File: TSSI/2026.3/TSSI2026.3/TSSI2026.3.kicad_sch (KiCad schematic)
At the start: 31 parts, among them J1 T2M-105-01-X-D-TH-DS, J2 Conn_01x02, Q1 IRLZ34N, T555 Test555, U1 LM555xN, U2 IRLZ34N, U3 IRLZ34N, U4 4001, U5 4069

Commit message: Change TSSI2026.3
Deleted the whole schematic ong
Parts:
- removed DEBUG1: BMS, LED_THT:LED_D4.0mm, symbol Device:LED
- removed DEBUG2: IMD, LED_THT:LED_D4.0mm, symbol Device:LED
- removed IMD1: TestIMD, Connector_PinHeader_1.00mm:PinHeader_1x01_P1.00mm_Vertical, symbol Connector:Conn_01x01_Pin
- removed J1: T2M-105-01-X-D-TH-DS, T2M-105-01-X-D-TH-DS:SAMTEC_T2M-105-01-X-D-TH-DS, symbol T2M-105-01-X-D-TH-DS:T2M-105-01-X-D-TH-DS
- removed R3: 50, Resistor_SMD:R_0805_2012Metric, symbol Device:R_US
- removed R9: 20k, Resistor_SMD:R_0805_2012Metric, symbol Device:R_US
- removed U2: IRLZ34N, Anteater-Electric-Racing electrical-pcbs main TSSI-2026.2_KiCad_Parts_IRLZ34N:TO-220_2_, symbol IRLZ34N:IRLZ34N
- removed U4: 4001, Package_SO:SOIC-14_3.9x8.7mm_P1.27mm, symbol 4xxx:4001
- removed U5: 4069, Package_SO:SOIC-14_3.9x8.7mm_P1.27mm, symbol 4xxx:4069
- added D1: DEBUGLatch, LED_THT:LED_D4.0mm, symbol Device:LED
- added J1: Conn_02x02, Connector_Molex:Molex_Mini-Fit_Jr_5566-04A2_2x02_P4.20mm_Vertical, symbol Connector_Generic:Conn_02x02_Counter_Clockwise
- added Q2, Q3: IRLZ34N, Anteater-Electric-Racing electrical-pcbs main TSSI-2026.2_KiCad_Parts_IRLZ34N:TO-220_2_, symbol IRLZ34N:IRLZ34N
- R1: value 22k -> 10k
- R2: value 20k -> 22k
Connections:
- net GLV: now also R1.1, J1.1 (Pin_1); no longer R1.2
- net GND: now also D1.1 (K), J1.2 (Pin_2), Q2.OUT, Q3.OUT
- net at Q1.IN: now also R1.2, Q2.IN, Q3.GND
- net at R5.2, U1.4 (R): now also Q2.GND
- net Latch_12V_Safe: now reaches R2.1
- net Latch_12V_Safe: now also BMS1.1 (Pin_1), J1.3 (Pin_3), Q3.IN
- removed net BMS_FAULT: BMS1.1 (Pin_1), R1.1
- net IMD_FAULT: no longer names the net of R2.2
- net IMD_FAULT: now also D1.2 (A)
- no-connect marks 7 -> 1
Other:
- moved on the sheet: BMS1, C1, C2, C3, GLV1, GND1, H1, H2, H3, H4, J2, Q1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

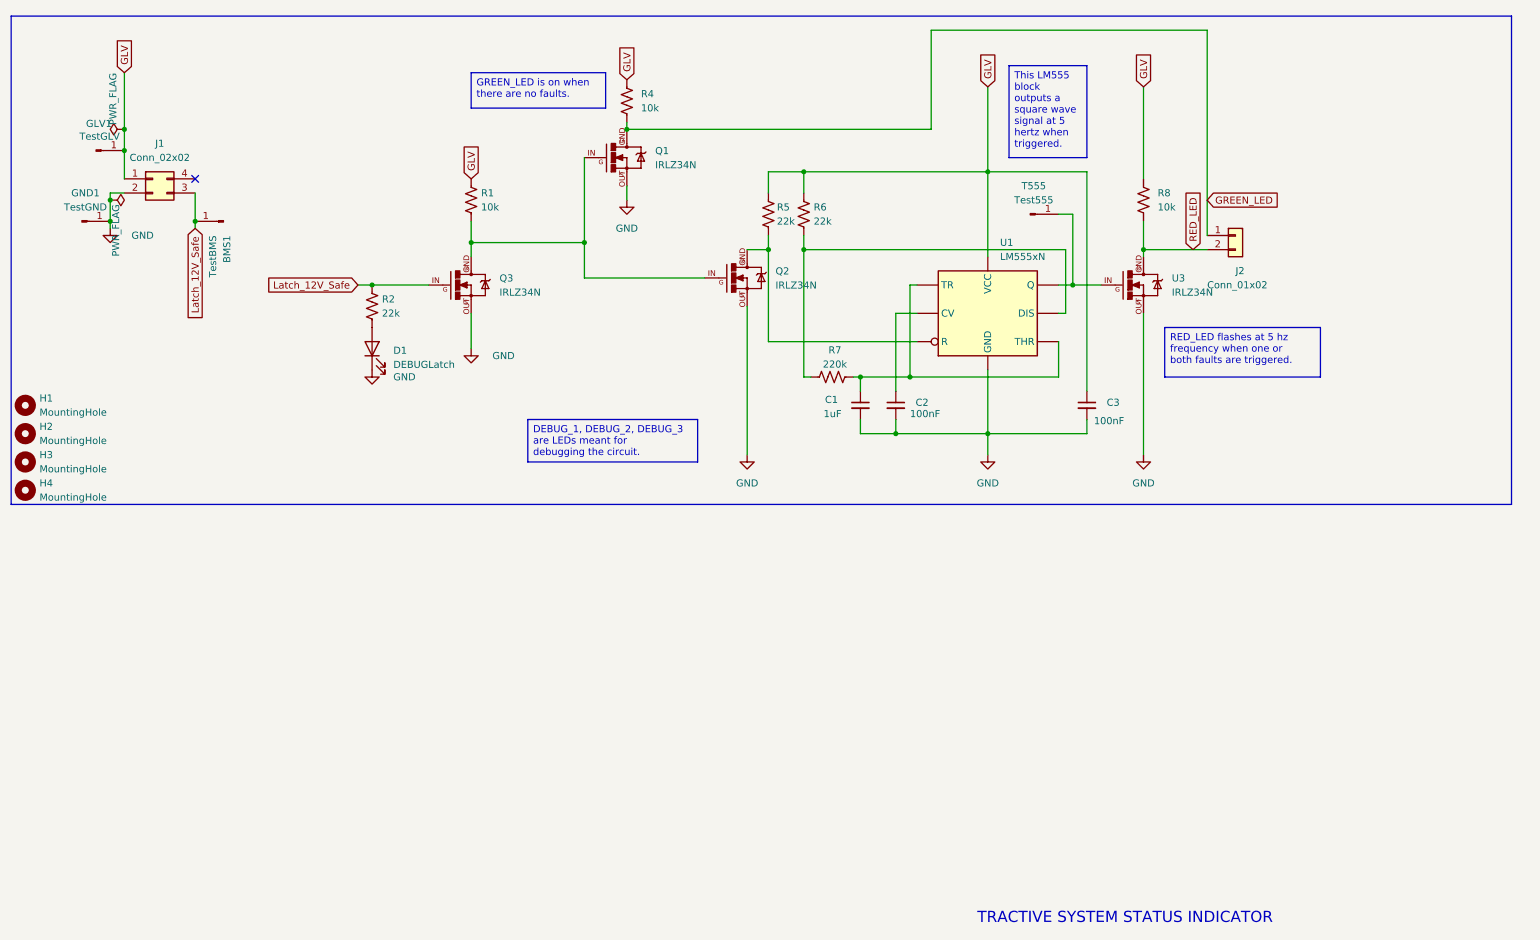
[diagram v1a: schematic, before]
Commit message: Redesign TSSI
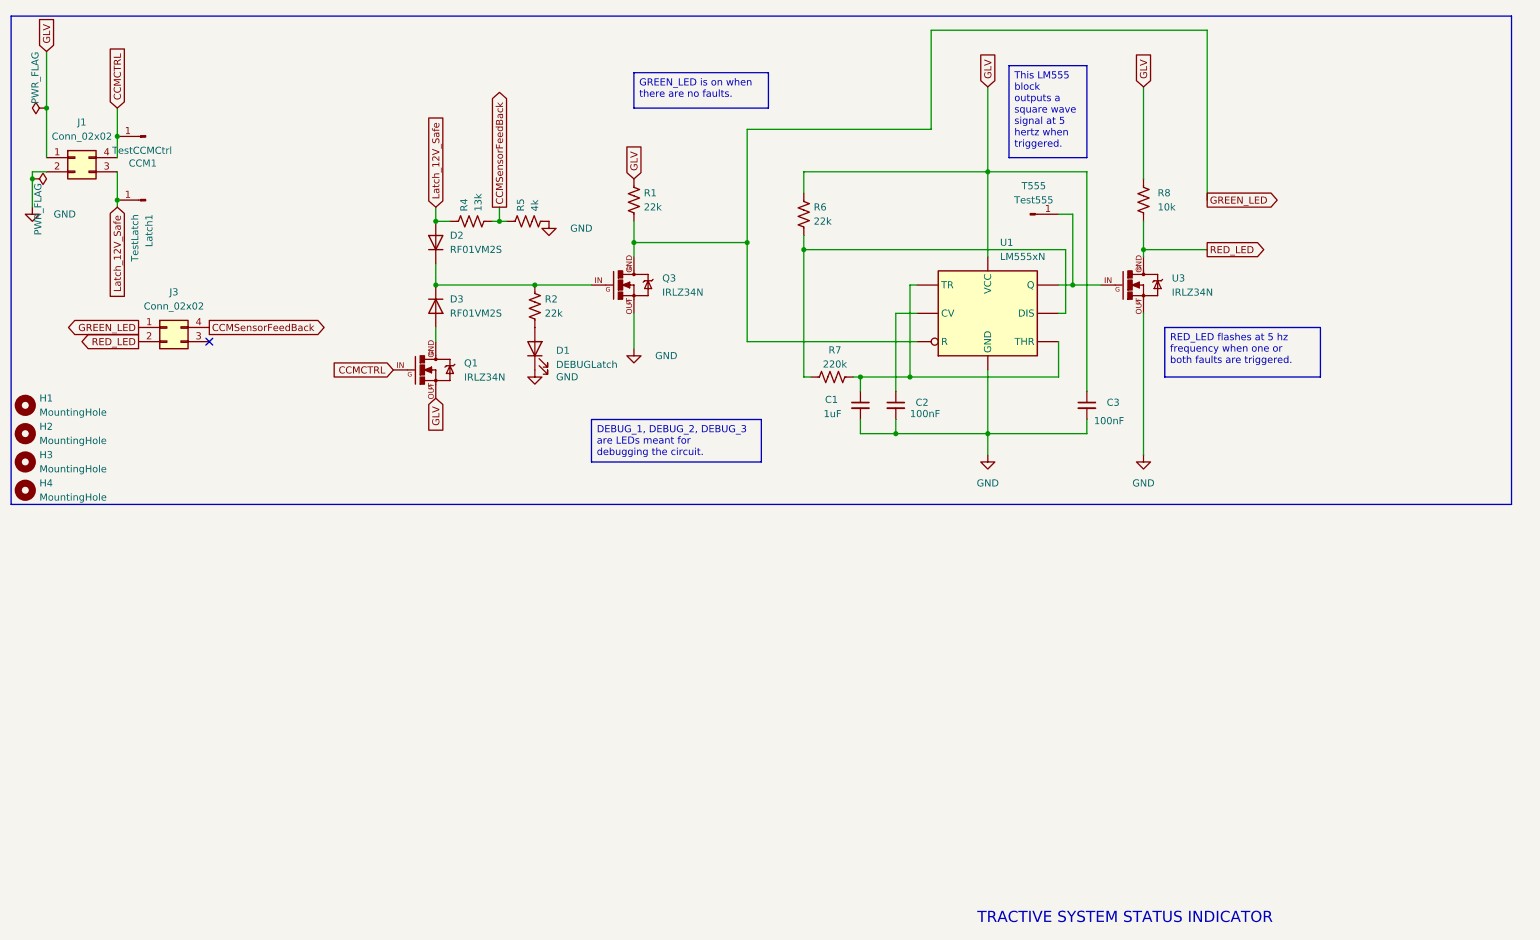
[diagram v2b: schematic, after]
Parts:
- removed GLV1: TestGLV, Connector_PinHeader_1.00mm:PinHeader_1x01_P1.00mm_Vertical, symbol Connector:Conn_01x01_Pin
- removed GND1: TestGND, Connector_PinHeader_1.00mm:PinHeader_1x01_P1.00mm_Vertical, symbol Connector:Conn_01x01_Pin
- removed J2: Conn_01x02, Connector_Molex:Molex_Mini-Fit_Jr_5566-02A_2x01_P4.20mm_Vertical, symbol Connector_Generic:Conn_01x02
- removed Q2: IRLZ34N, Anteater-Electric-Racing electrical-pcbs main TSSI-2026.2_KiCad_Parts_IRLZ34N:TO-220_2_, symbol IRLZ34N:IRLZ34N
- added CCM1: TestCCMCtrl, Connector_PinHeader_1.00mm:PinHeader_1x01_P1.00mm_Vertical, symbol Connector:Conn_01x01_Pin
- added D2, D3: RF01VM2S, Diode_SMD:D_0805_2012Metric, symbol Diode:RF01VM2S
- added J3: Conn_02x02, Connector_Molex:Molex_Mini-Fit_Jr_5566-04A2_2x02_P4.20mm_Vertical, symbol Connector_Generic:Conn_02x02_Counter_Clockwise
- Latch1: renamed from BMS1; value TestBMS -> TestLatch
- R1: value 10k -> 22k
- R4: value 10k -> 13k
- R5: value 22k -> 4k
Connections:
- net GLV: now also Q1.OUT; no longer R4.1, R5.1
- net GND: now also R5.2; no longer Q1.OUT
- net GREEN_LED: now also Q3.GND, R1.2, U1.4 (R), J3.1 (Pin_1); no longer Q1.GND, R4.2
- net Latch_12V_Safe: now also R4.1, D2.2 (A); no longer Q3.IN, R2.1
- net RED_LED: now also J3.2 (Pin_2)
- net CCMCTRL: now reaches J1.4 (Pin_4)
- net CCMCTRL: now also Q1.IN, CCM1.1 (Pin_1)
- new net: D3.2 (A), Q1.GND
- new net: D2.1 (K), D3.1 (K), Q3.IN, R2.1
- new net CCMSensorFeedBack: J3.4 (Pin_4), R4.2, R5.1
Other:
- moved on the sheet: D1, J1, Latch1, Q3, R1, R2

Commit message: Swapped NMOS at bottom
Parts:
- Q1, Q3, U3: footprint Anteater-Electric-Racing electrical-pcbs main TSSI-2026.2_KiCad_Parts_IRLZ34N:TO-220_2_ -> IRLZ34N:TO-220_2_
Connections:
- net GLV: now also Q1.GND; no longer Q1.OUT
- net at D3.2 (A): now also Q1.OUT; no longer Q1.GND
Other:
- moved on the sheet: D2, D3, Q1
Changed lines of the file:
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@@
 	)
 	(junction
-		(at 90.17 62.23)
+		(at 82.55 62.23)
 		(diameter 0)
 		(color 0 0 0 0)
@@
 	)
 	(junction
-		(at 90.17 50.8)
+		(at 82.55 50.8)
 		(diameter 0)
 		(color 0 0 0 0)
@@
 	(wire
 		(pts
-			(xy 90.17 48.26) (xy 90.17 50.8)
+			(xy 82.55 48.26) (xy 82.55 50.8)
 		)
 		(stroke
@@
 	(wire
 		(pts
-			(xy 90.17 69.85) (xy 90.17 72.39)
+			(xy 82.55 69.85) (xy 82.55 72.39)
 		)
 		(stroke
@@
 	(wire
 		(pts
-			(xy 90.17 62.23) (xy 107.95 62.23)
+			(xy 82.55 62.23) (xy 107.95 62.23)
 		)
 		(stroke
@@
 	(wire
 		(pts
-			(xy 90.17 50.8) (xy 92.71 50.8)
+			(xy 82.55 50.8) (xy 92.71 50.8)
 		)
 		(stroke
@@
 	(wire
 		(pts
-			(xy 90.17 58.42) (xy 90.17 62.23)
+			(xy 82.55 58.42) (xy 82.55 62.23)
 		)
 		(stroke
@@
 	(global_label "CCMCTRL"
 		(shape input)
-		(at 82.55 77.47 180)
+		(at 90.17 77.47 0)
 		(fields_autoplaced yes)
 		(effects
@@
 				(size 1.27 1.27)
 			)
-			(justify right)
+			(justify left)
 		)
 		(property "Intersheetrefs" "${INTERSHEET_REFS}"
-			(at 71.0377 77.47 0)
-			(effects
-				(font
-					(size 1.27 1.27)
-				)
-				(justify right)
+			(at 101.6823 77.47 0)
+			(effects
+				(font
+					(size 1.27 1.27)
+				)
+				(justify left)
 				(hide yes)
 			)
@@
 	(global_label "Latch_12V_Safe"
 		(shape input)
-		(at 90.17 48.26 90)
+		(at 82.55 48.26 90)
 		(fields_autoplaced yes)
 		(effects
@@
 		)
 		(property "Intersheetrefs" "${INTERSHEET_REFS}"
-			(at 90.17 30.5188 90)
+			(at 82.55 30.5188 90)
 			(effects
 				(font
@@
 	(global_label "GLV"
 		(shape input)
-		(at 90.17 82.55 270)
+		(at 82.55 82.55 270)
 		(fields_autoplaced yes)
 		(effects
@@
 		)
 		(property "Intersheetrefs" "${INTERSHEET_REFS}"
-			(at 90.17 88.9219 90)
+			(at 82.55 88.9219 90)
 			(effects
 				(font
@@
 		(lib_name "IRLZ34N_1")
 		(lib_id "IRLZ34N:IRLZ34N")
-		(at 90.17 77.47 0)
+		(at 82.55 77.47 180)
 		(unit 1)
 		(exclude_from_sim no)
@@
 		(fields_autoplaced yes)
 		(property "Reference" "Q1"
-			(at 95.25 76.2484 0)
+			(at 77.47 76.1514 0)
 			(effects
 				(font
@@
 		)
 		(property "Value" "IRLZ34N"
-			(at 95.25 78.7884 0)
-			(effects
-				(font
-					(size 1.27 1.27)
-				)
-				(justify left)
-			)
-		)
-		(property "Footprint" "Anteater-Electric-Racing electrical-pcbs main TSSI-2026.2_KiCad_Parts_IRLZ34N:TO-220_2_"
-			(at 90.17 77.47 0)
+			(at 77.47 78.6914 0)
+			(effects
+				(font
+					(size 1.27 1.27)
+				)
+				(justify left)
+			)
+		)
+		(property "Footprint" "IRLZ34N:TO-220_2_"
+			(at 82.55 77.47 0)
 			(effects
 				(font
@@
 		)
 		(property "Datasheet" ""
-			(at 90.17 77.47 0)
+			(at 82.55 77.47 0)
 			(effects
 				(font
@@
 		)
 		(property "Description" ""
-			(at 90.17 77.47 0)
+			(at 82.55 77.47 0)
 			(effects
 				(font
@@
 		)
 		(property "MF" "Infineon"
-			(at 90.17 77.47 0)
+			(at 82.55 77.47 0)
 			(effects
 				(font
@@
 		)
 		(property "Description_1" "N-Channel 55 V 30A (Tc) 3.8W (Ta), 68W (Tc) Surface Mount D2PAK"
-			(at 90.17 77.47 0)
+			(at 82.55 77.47 0)
 			(effects
 				(font
@@
 		)
 		(property "Package" "TO-220 Infineon"
-			(at 90.17 77.47 0)
+			(at 82.55 77.47 0)
 			(effects
 				(font
@@
 		)
 		(property "Price" "None"
-			(at 90.17 77.47 0)
+			(at 82.55 77.47 0)
 			(effects
 				(font
@@
 		)
 		(property "SnapEDA_Link" "https://www.snapeda.com/parts/IRLZ34N/Infineon/view-part/?ref=snap"
-			(at 90.17 77.47 0)
+			(at 82.55 77.47 0)
 			(effects
 				(font
@@
 		)
 		(property "MP" "IRLZ34N"
-			(at 90.17 77.47 0)
+			(at 82.55 77.47 0)
 			(effects
 				(font
@@
 		)
 		(property "Purchase-URL" "https://www.snapeda.com/api/url_track_click_mouser/?unipart_id=346822&manufacturer=Infineon&part_name=IRLZ34N&search_term=None"
-			(at 90.17 77.47 0)
+			(at 82.55 77.47 0)
 			(effects
 				(font
@@
 		)
 		(property "Availability" "In Stock"
-			(at 90.17 77.47 0)
+			(at 82.55 77.47 0)
 			(effects
 				(font
@@
 		)
 		(property "Check_prices" "https://www.snapeda.com/parts/IRLZ34N/Infineon/view-part/?ref=eda"
-			(at 90.17 77.47 0)
+			(at 82.55 77.47 0)
 			(effects
 				(font
@@
 			)
 		)
-		(property "Footprint" "Anteater-Electric-Racing electrical-pcbs main TSSI-2026.2_KiCad_Parts_IRLZ34N:TO-220_2_"
+		(property "Footprint" "IRLZ34N:TO-220_2_"
 			(at 217.17 62.23 0)
 			(effects
@@
 			)
 		)
-		(property "Footprint" "Anteater-Electric-Racing electrical-pcbs main TSSI-2026.2_KiCad_Parts_IRLZ34N:TO-220_2_"
+		(property "Footprint" "IRLZ34N:TO-220_2_"
 			(at 125.73 62.23 0)
 			(effects
@@
 	(symbol
 		(lib_id "Diode:RF01VM2S")
-		(at 90.17 66.04 270)
+		(at 82.55 66.04 270)
 		(unit 1)
 		(exclude_from_sim no)
@@
 		(fields_autoplaced yes)
 		(property "Reference" "D3"
-			(at 92.71 64.7699 90)
+			(at 85.09 64.7699 90)
 			(effects
 				(font
@@
 		)
 		(property "Value" "RF01VM2S"
-			(at 92.71 67.3099 90)
+			(at 85.09 67.3099 90)
 			(effects
 				(font
@@
 		)
 		(property "Footprint" "Diode_SMD:D_0805_2012Metric"
-			(at 90.17 66.04 0)
+			(at 82.55 66.04 0)
 			(effects
 				(font
@@
 		)
 		(property "Datasheet" "https://fscdn.rohm.com/en/products/databook/datasheet/discrete/diode/fast_recovery/rf01vm2s.pdf"
-			(at 90.17 66.04 0)
+			(at 82.55 66.04 0)
 			(effects
 				(font
@@
 		)
 		(property "Description" "250 V, 100 mA, Super Fast Recovery Diode, SOD-323"
-			(at 90.17 66.04 0)
+			(at 82.55 66.04 0)
 			(effects
 				(font
@@
 		)
 		(property "Sim.Device" "D"
-			(at 90.17 66.04 0)
+			(at 82.55 66.04 0)
 			(effects
 				(font
@@
 		)
 		(property "Sim.Pins" "1=K 2=A"
-			(at 90.17 66.04 0)
+			(at 82.55 66.04 0)
 			(effects
 				(font
@@
 	(symbol
 		(lib_id "Diode:RF01VM2S")
-		(at 90.17 54.61 90)
+		(at 82.55 54.61 90)
 		(unit 1)
 		(exclude_from_sim no)
@@
 		(fields_autoplaced yes)
 		(property "Reference" "D2"
-			(at 92.71 53.3399 90)
+			(at 85.09 53.3399 90)
 			(effects
 				(font
@@
 		)
 		(property "Value" "RF01VM2S"
-			(at 92.71 55.8799 90)
+			(at 85.09 55.8799 90)
 			(effects
 				(font
@@
 		)
 		(property "Footprint" "Diode_SMD:D_0805_2012Metric"
-			(at 90.17 54.61 0)
+			(at 82.55 54.61 0)
 			(effects
 				(font
@@
 		)
 		(property "Datasheet" "https://fscdn.rohm.com/en/products/databook/datasheet/discrete/diode/fast_recovery/rf01vm2s.pdf"
-			(at 90.17 54.61 0)
+			(at 82.55 54.61 0)
 			(effects
 				(font
@@
 		)
 		(property "Description" "250 V, 100 mA, Super Fast Recovery Diode, SOD-323"
-			(at 90.17 54.61 0)
+			(at 82.55 54.61 0)
 			(effects
 				(font
@@
 		)
 		(property "Sim.Device" "D"
-			(at 90.17 54.61 0)
+			(at 82.55 54.61 0)
 			(effects
 				(font
@@
 		)
 		(property "Sim.Pins" "1=K 2=A"
-			(at 90.17 54.61 0)
-			(effects
-				(font
+			(at 82.55 54.61 0)
+			(effects
+				(font
